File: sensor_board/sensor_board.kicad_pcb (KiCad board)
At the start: 2 copper layers, 26.2 x 20.3 mm, 10 parts, among them J1 Comm, J2 OUTPUT, J3 INPUT, U1 INA228

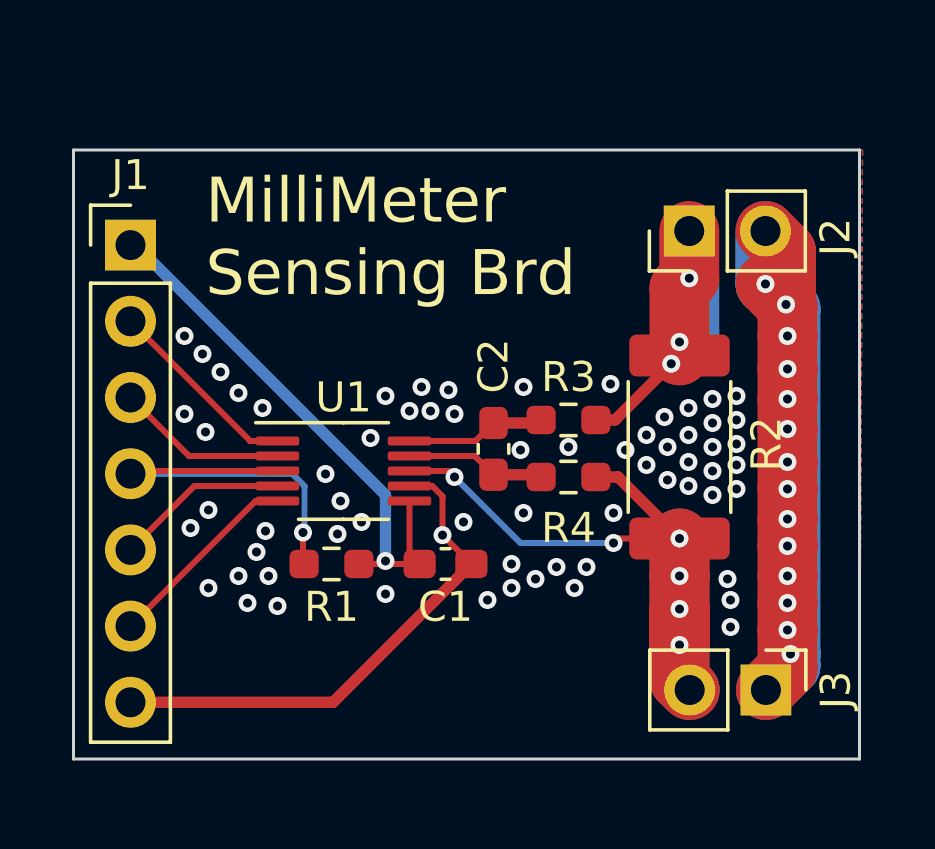
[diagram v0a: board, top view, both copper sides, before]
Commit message: Rename INA228 sensor board
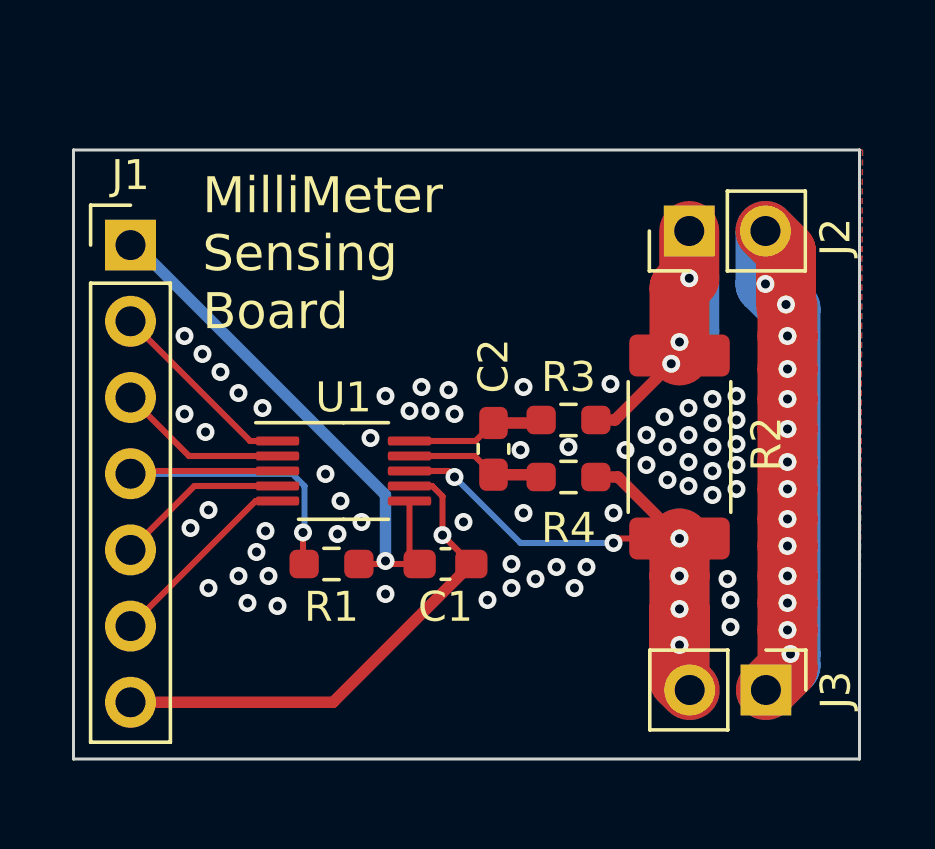
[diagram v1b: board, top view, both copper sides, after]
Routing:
- net Net-(J2-Pad2): track 32.9 -> 31.8 mm
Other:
- board text added: "MilliMeter Sensing Board"
- board text removed: "MilliMeter Sensing Brd"
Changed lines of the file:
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@@
     (effects (font (size 1 1) (thickness 0.15)) (justify mirror))
   )
-  (gr_text "MilliMeter \nSensing Brd" (at 117.8 67.7) (layer "F.SilkS")
-    (effects (font (size 1.5 1.5) (thickness 0.2)) (justify left))
+  (gr_text "MilliMeter \nSensing\nBoard" (at 117.7 68.25) (layer "F.SilkS")
+    (effects (font (size 1.2 1.2) (thickness 0.2)) (justify left))
   )
   (segment (start 125.357593 76) (end 125.7 76.342407) (width 0.2032) (layer "F.Cu") (net 1))
@@
   (segment (start 133.6 82.46) (end 133.94 82.8) (width 2) (layer "F.Cu") (net 10))
   (segment (start 131.55 75.7) (end 133.6 77.75) (width 0.381) (layer "F.Cu") (net 10))
-  (segment (start 133.5 77.65) (end 133.4 77.75) (width 0.508) (layer "F.Cu") (net 10))
   (segment (start 133.6 79) (end 133.6 80.1) (width 2) (layer "F.Cu") (net 10))
   (segment (start 133.6 80.1) (end 133.6 81.3) (width 2) (layer "F.Cu") (net 10))
@@
   (segment (start 137.2 73.1) (end 137.2 74.1) (width 2) (layer "F.Cu") (net 11))
   (segment (start 137.2 72.1) (end 137.2 73.1) (width 2) (layer "F.Cu") (net 11))
-  (segment (start 136.465 69.265) (end 137.15 69.95) (width 2) (layer "F.Cu") (net 11))
   (segment (start 137.2 74.1) (end 137.2 75.2) (width 2) (layer "F.Cu") (net 11))
   (segment (start 137.2 75.2) (end 137.2 76.1) (width 2) (layer "F.Cu") (net 11))
   (segment (start 137.2 79) (end 137.2 79.9) (width 2) (layer "F.Cu") (net 11))
-  (segment (start 137.15 69.95) (end 137.2 70) (width 2) (layer "F.Cu") (net 11))
   (segment (start 137.2 76.1) (end 137.2 77.1) (width 2) (layer "F.Cu") (net 11))
   (segment (start 137.2 78) (end 137.2 79) (width 2) (layer "F.Cu") (net 11))

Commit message: sensor_board: rev 1.1
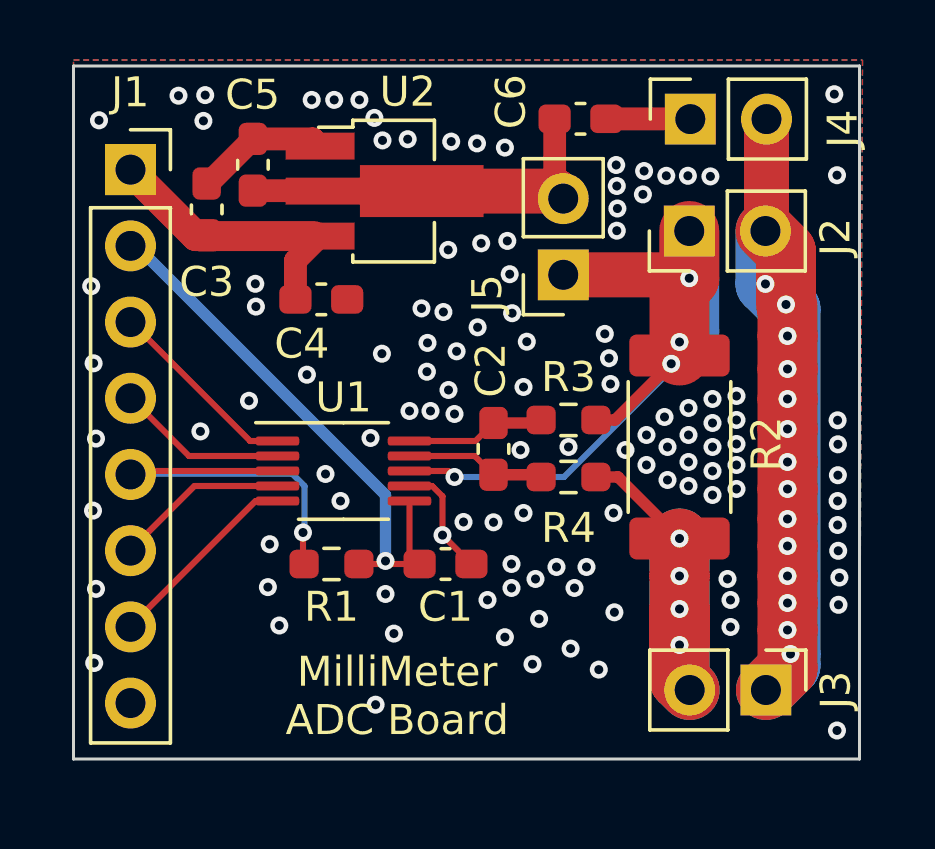
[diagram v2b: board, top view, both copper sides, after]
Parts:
- added C3: 10uF, Capacitor_SMD:C_0603_1608Metric_Pad1.08x0.95mm_HandSolder, F.Cu at (117.8, 66.8)
- added C4: 0.1uF, Capacitor_SMD:C_0603_1608Metric_Pad1.08x0.95mm_HandSolder, F.Cu at (121.7, 69.8)
- added C5: 0.1uF, Capacitor_SMD:C_0603_1608Metric_Pad1.08x0.95mm_HandSolder, F.Cu at (119.4, 65.3)
- added C6: 10uF, Capacitor_SMD:C_0603_1608Metric_Pad1.08x0.95mm_HandSolder, F.Cu at (130.3, 63.8)
- added J4: LDO_GND, Connector_PinSocket_2.54mm:PinSocket_1x02_P2.54mm_Vertical, F.Cu at (134.0, 63.8)
- added J5: LDO_VCC, Connector_PinSocket_2.54mm:PinSocket_1x02_P2.54mm_Vertical, F.Cu at (129.7, 69.0)
- added U2: AMS1117/WL9005P3, Package_TO_SOT_SMD:SOT-89-3_Handsoldering, F.Cu at (123.8, 66.2)
- J1: footprint Connector_PinHeader_2.54mm:PinHeader_1x07_P2.54mm_Vertical -> Connector_PinSocket_2.54mm:PinSocket_1x08_P2.54mm_Vertical
- moved J1 2.52 mm to (115.3, 65.5)
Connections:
- J1 pad 1: +3V3 -> +5V
- J1 pad 2: A1 -> +3V3
- J1 pad 3: A0 -> A1
- J1 pad 4: ALERT -> A0
- J1 pad 5: SDA -> ALERT
- J1 pad 6: SCL -> SDA
- J1 pad 7: GND -> SCL
- J2 pad 1: Net-(J2-Pad1) -> VBUS
- J3 pad 2: VBUS -> Net-(J3-Pad2)
- R2 pad 1: VBUS -> Net-(J3-Pad2)
- R2 pad 2: Net-(J2-Pad1) -> VBUS
- R3 pad 2: Net-(J2-Pad1) -> VBUS
- R4 pad 2: VBUS -> Net-(J3-Pad2)
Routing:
- net Net-(J3-Pad2): track 0.00 -> 15.2 mm, vias 0 -> 4
- net +3.3VADC: track 0.00 -> 11.1 mm
- net Net-(J2-Pad1): track 10.2 -> 0.00 mm, vias 3 -> 0
- net +5V: track 0.00 -> 9.51 mm
- net GND: track 17.2 -> 11.2 mm, vias 66 -> 117
- net Net-(J2-Pad2): track 31.8 -> 35.6 mm
- net VBUS: track 25.3 -> 25.6 mm, vias 6 -> 4
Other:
- board size 26.2 x 20.3 mm -> 26.2 x 23.1 mm
- board text added: "<<<<<<<<"
- board text added: "Copyright (C) 2023 Jackson M Hu Rev 1"
- board text added: "LDO_GND"
- board text added: "LDO_Vext"
- board text added: "MilliMeter ADC Board"
- board text added: "Vext 3v3 A1 A0 ALERT SDA SCL GND"
- board text removed: "(C) 2022 Jackson M Hu Rev 1"
- board text removed: "---->>"
- board text removed: "3v3 A1 A0 ALERT SDA SCL GND"
- board text removed: "MilliMeter Sensing Board"

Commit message: Generate Rev. 1 gerber
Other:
- board size 26.2 x 23.1 mm -> 27 x 24 mm
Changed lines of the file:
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@@
     )
   )
-  (gr_line (start 113.4 62) (end 139.6 62) (layer "Edge.Cuts") (width 0.1))
-  (gr_line (start 113.4 85.1) (end 113.4 62) (layer "Edge.Cuts") (width 0.1))
-  (gr_line (start 139.6 85.1) (end 113.4 85.1) (layer "Edge.Cuts") (width 0.1))
-  (gr_line (start 139.6 62) (end 139.6 85.1) (layer "Edge.Cuts") (width 0.1))
+  (gr_line (start 113 62) (end 140 62) (layer "Edge.Cuts") (width 0.1))
+  (gr_line (start 113 86) (end 113 62) (layer "Edge.Cuts") (width 0.1))
+  (gr_line (start 140 86) (end 113 86) (layer "Edge.Cuts") (width 0.1))
+  (gr_line (start 140 62) (end 140 86) (layer "Edge.Cuts") (width 0.1))
   (gr_text "Vext\n3v3\nA1\nA0\nALERT\nSDA\nSCL\nGND" (at 116.61 74.31) (layer "B.SilkS")
     (effects (font (size 1.6 1) (thickness 0.2)) (justify right mirror))
@@
     (polygon
       (pts
-        (xy 139.6 85.1)
-        (xy 113.4 85.1)
-        (xy 113.4 61.8)
-        (xy 139.7 61.8)
+        (xy 139.940069 86.101461)
+        (xy 113.019946 86.1)
+        (xy 113.02 61.8)
+        (xy 140.040123 61.801461)
       )
     )
